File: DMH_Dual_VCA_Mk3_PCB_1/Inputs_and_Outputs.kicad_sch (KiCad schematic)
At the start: 24 parts, among them J1 TS_Jack_6.35mm_Sw, J2 TS_Jack_6.35mm_Sw, J200 IDC_02x05, J3 TS_Jack_6.35mm_Sw, J4 TS_Jack_6.35mm_Sw, J5 TS_Jack_6.35mm_Sw, J50 Conn_01x08, J6 TS_Jack_6.35mm_Sw, J60 Conn_01x08, J7 TS_Jack_6.35mm_Sw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

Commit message: Mode switching design in progress
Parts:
- removed D3: ZPD5V1, Diode_THT:D_DO-35_SOD27_P7.62mm_Horizontal, symbol Diode:ZPDxx
- removed R2: 4k7, Resistor_THT:R_Axial_DIN0207_L6.3mm_D2.5mm_P7.62mm_Horizontal, symbol Device:R_US
- R21, R40: value 20k -> 18k
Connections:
- net +5V: now reaches JP1.3 (B)

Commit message: 2nd VCA design done
Clipping design in progress
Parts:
- removed RV13: 100k, SynthStuff:Potentiometer_Alpha_RD901F-40-00D_Single_Vertical, symbol Device:R_Potentiometer_US
- added RV13: 100k, symbol Device:R_Potentiometer_Dual_Separate
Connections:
- net +5V: now also RV13.6
- net GND: now also RV13.1
- net CV P/T Jack renamed CV PT In Jack
- net CV PT In Jack: now also RV13.3
- new net -5V: RV13.4
- new net CV PT Pot G1: RV13.2
- new net CV PT Pot G2: RV13.5

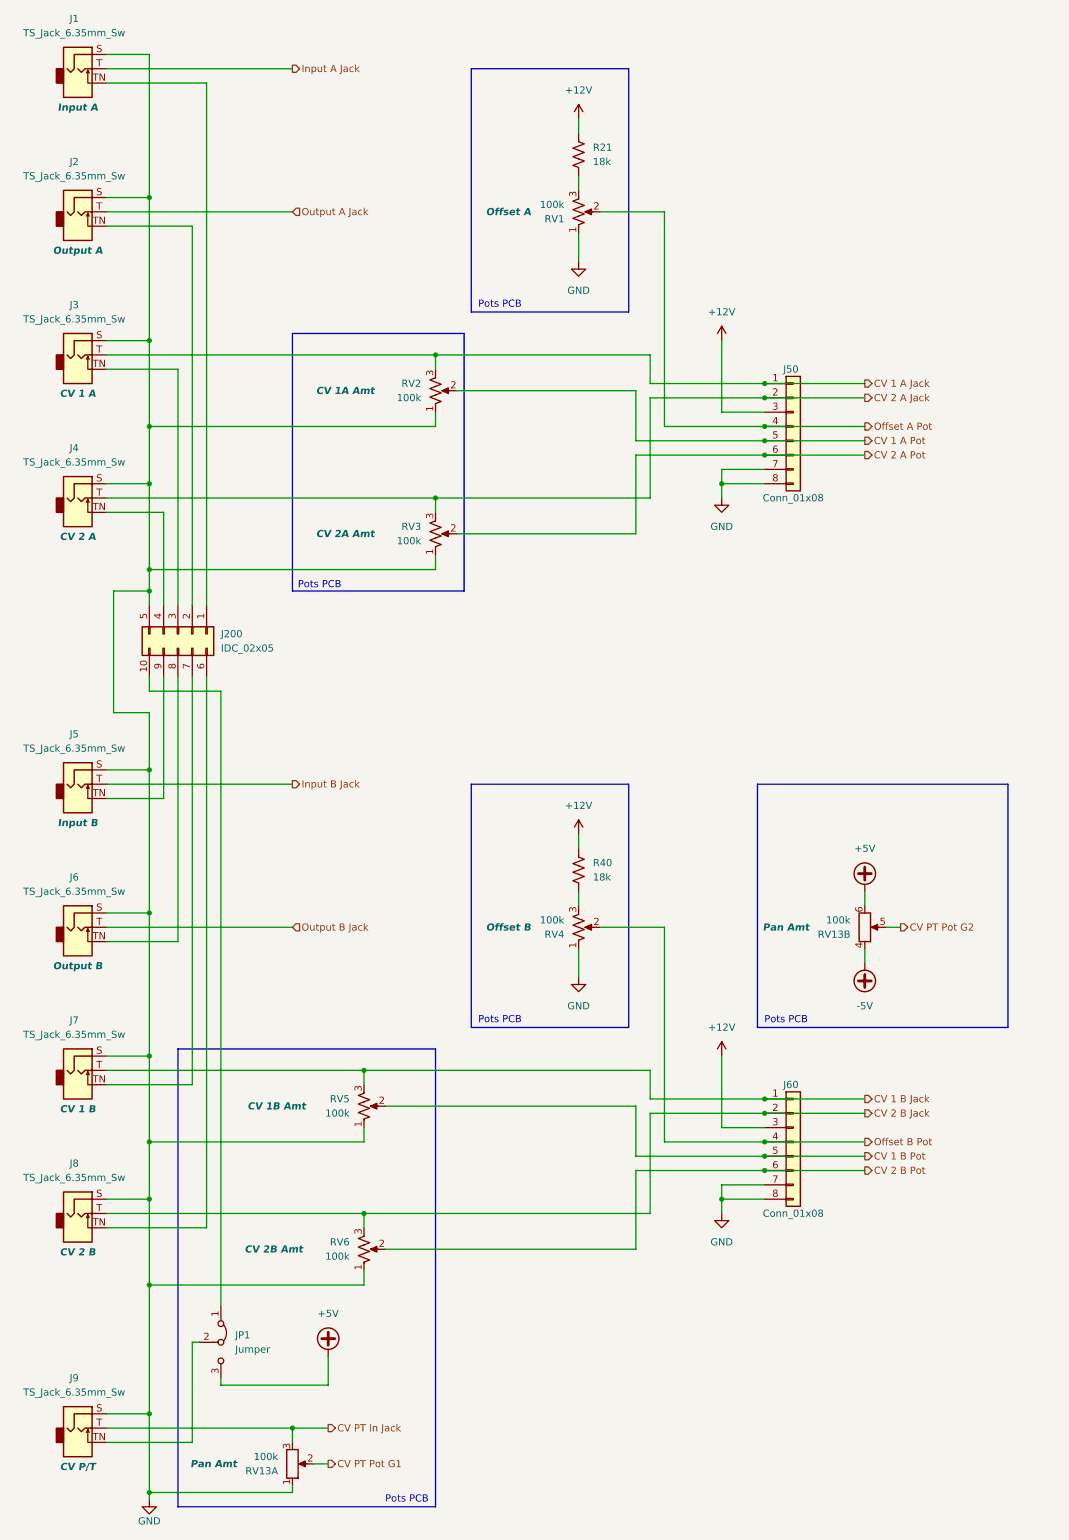
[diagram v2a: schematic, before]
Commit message: Designed clip and dist circuit
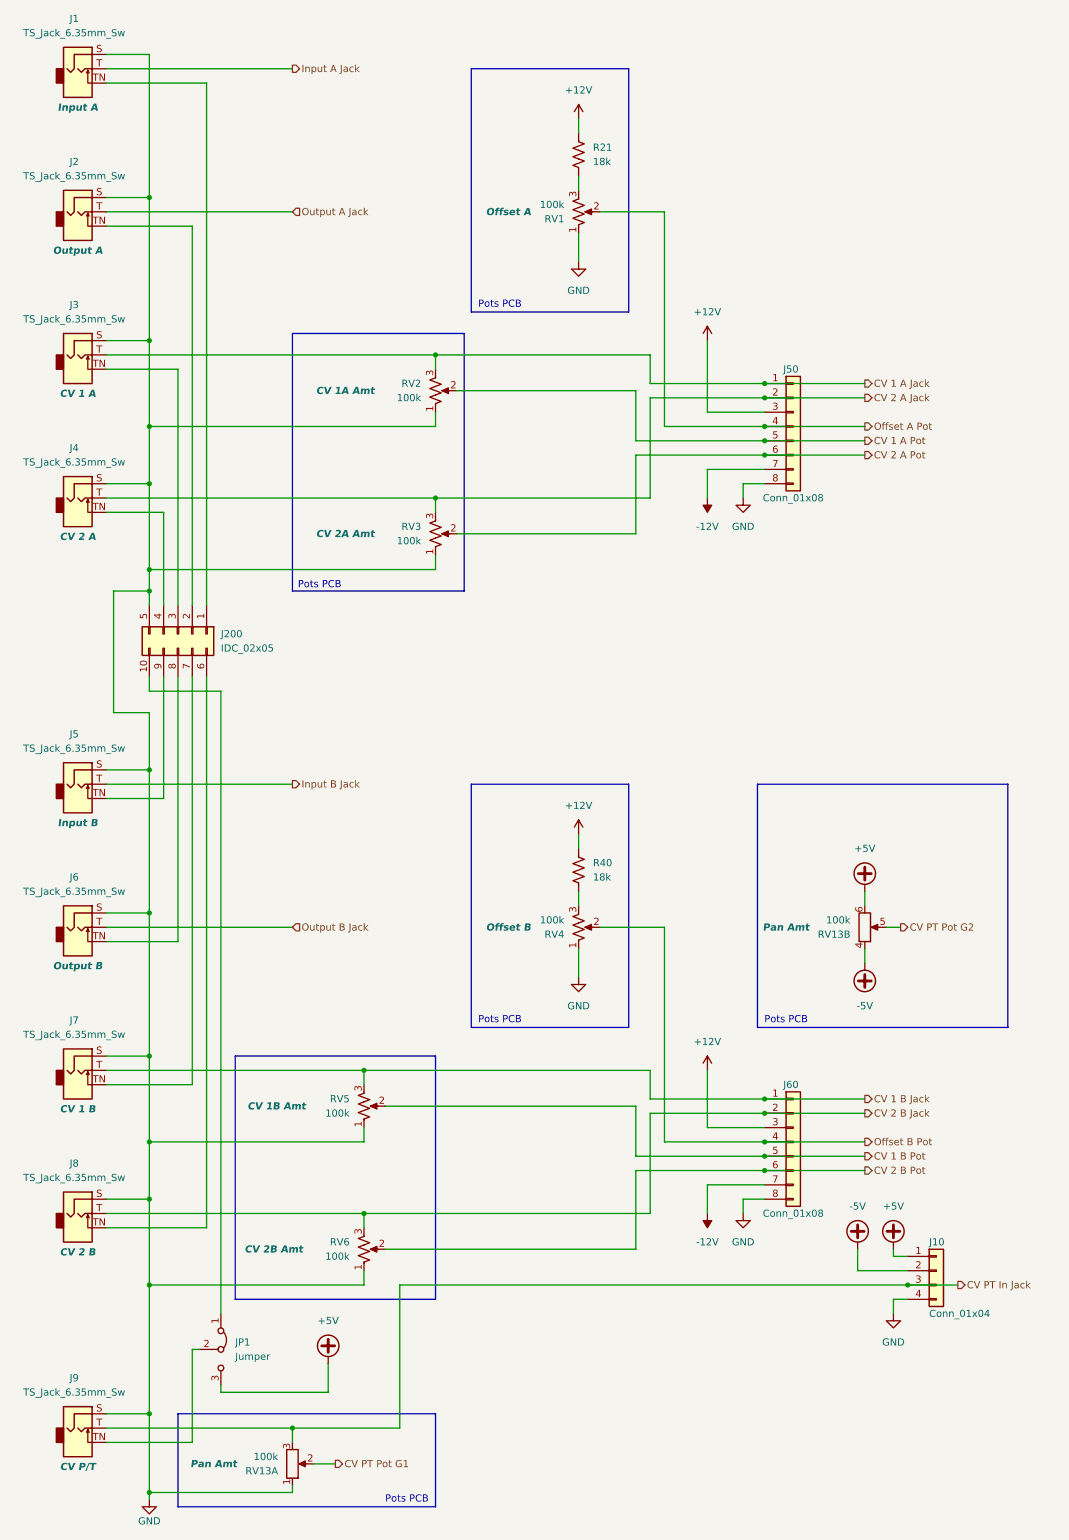
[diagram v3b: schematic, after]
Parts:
- added J10: Conn_01x04, Connector_PinHeader_2.54mm:PinHeader_1x04_P2.54mm_Vertical, symbol Connector_Generic:Conn_01x04
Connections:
- net +5V: now also J10.1 (Pin_1)
- net -5V: now also J10.2 (Pin_2)
- net CV PT In Jack: now also J10.3 (Pin_3)
- net GND: now also J10.4 (Pin_4); no longer J50.7 (Pin_7), J60.7 (Pin_7)
- new net -12V: J50.7 (Pin_7), J60.7 (Pin_7)
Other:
- moved on the sheet: JP1

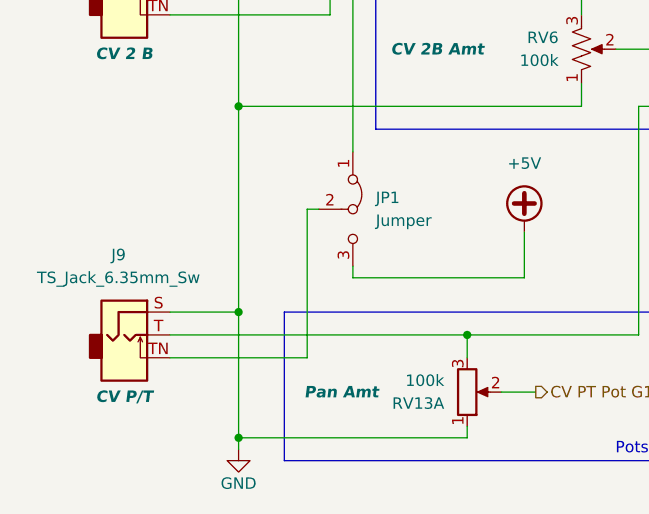
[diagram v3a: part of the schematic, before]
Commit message: Synced PCB 1 and 2 schematics
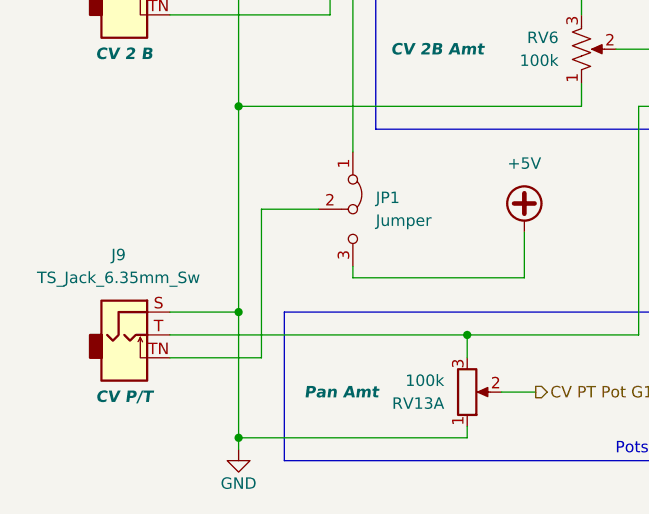
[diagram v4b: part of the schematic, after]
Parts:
- J50, J60: footprint Connector_PinSocket_2.54mm:PinSocket_1x08_P2.54mm_Vertical -> Connector_PinHeader_2.54mm:PinHeader_1x08_P2.54mm_Vertical
- JP1: footprint (none) -> Connector_PinHeader_2.54mm:PinHeader_1x03_P2.54mm_Horizontal
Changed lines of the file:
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@@
 	(wire
 		(pts
-			(xy 45.72 252.73) (xy 45.72 269.24)
+			(xy 40.64 252.73) (xy 40.64 269.24)
 		)
 		(stroke
@@
 	(wire
 		(pts
-			(xy 46.99 252.73) (xy 45.72 252.73)
+			(xy 46.99 252.73) (xy 40.64 252.73)
 		)
 		(stroke
@@
 	(wire
 		(pts
-			(xy 30.48 269.24) (xy 45.72 269.24)
+			(xy 30.48 269.24) (xy 40.64 269.24)
 		)
 		(stroke
@@
 		(exclude_from_sim no)
 		(in_bom yes)
-		(on_board yes)
+		(on_board no)
 		(dnp no)
 		(property "Reference" "RV13"
@@
 		(exclude_from_sim no)
 		(in_bom yes)
-		(on_board yes)
+		(on_board no)
 		(dnp no)
 		(property "Reference" "RV5"
@@
 		(exclude_from_sim no)
 		(in_bom yes)
-		(on_board yes)
+		(on_board no)
 		(dnp no)
 		(property "Reference" "RV6"
@@
 			)
 		)
-		(property "Footprint" "Connector_PinSocket_2.54mm:PinSocket_1x08_P2.54mm_Vertical"
+		(property "Footprint" "Connector_PinHeader_2.54mm:PinHeader_1x08_P2.54mm_Vertical"
 			(at 152.4 215.9 0)
 			(effects
@@
 		(exclude_from_sim no)
 		(in_bom yes)
-		(on_board yes)
+		(on_board no)
 		(dnp no)
 		(fields_autoplaced yes)
@@
 		(exclude_from_sim no)
 		(in_bom yes)
-		(on_board yes)
+		(on_board no)
 		(dnp no)
 		(fields_autoplaced yes)
@@
 		(exclude_from_sim no)
 		(in_bom yes)
-		(on_board yes)
+		(on_board no)
 		(dnp no)
 		(property "Reference" "RV13"
@@
 			)
 		)
-		(property "Footprint" "Connector_PinSocket_2.54mm:PinSocket_1x08_P2.54mm_Vertical"
+		(property "Footprint" "Connector_PinHeader_2.54mm:PinHeader_1x08_P2.54mm_Vertical"
 			(at 152.4 88.9 0)
 			(effects
@@
 			)
 		)
-		(property "Footprint" ""
+		(property "Footprint" "Connector_PinHeader_2.54mm:PinHeader_1x03_P2.54mm_Horizontal"
 			(at 50.8 252.73 0)
 			(effects

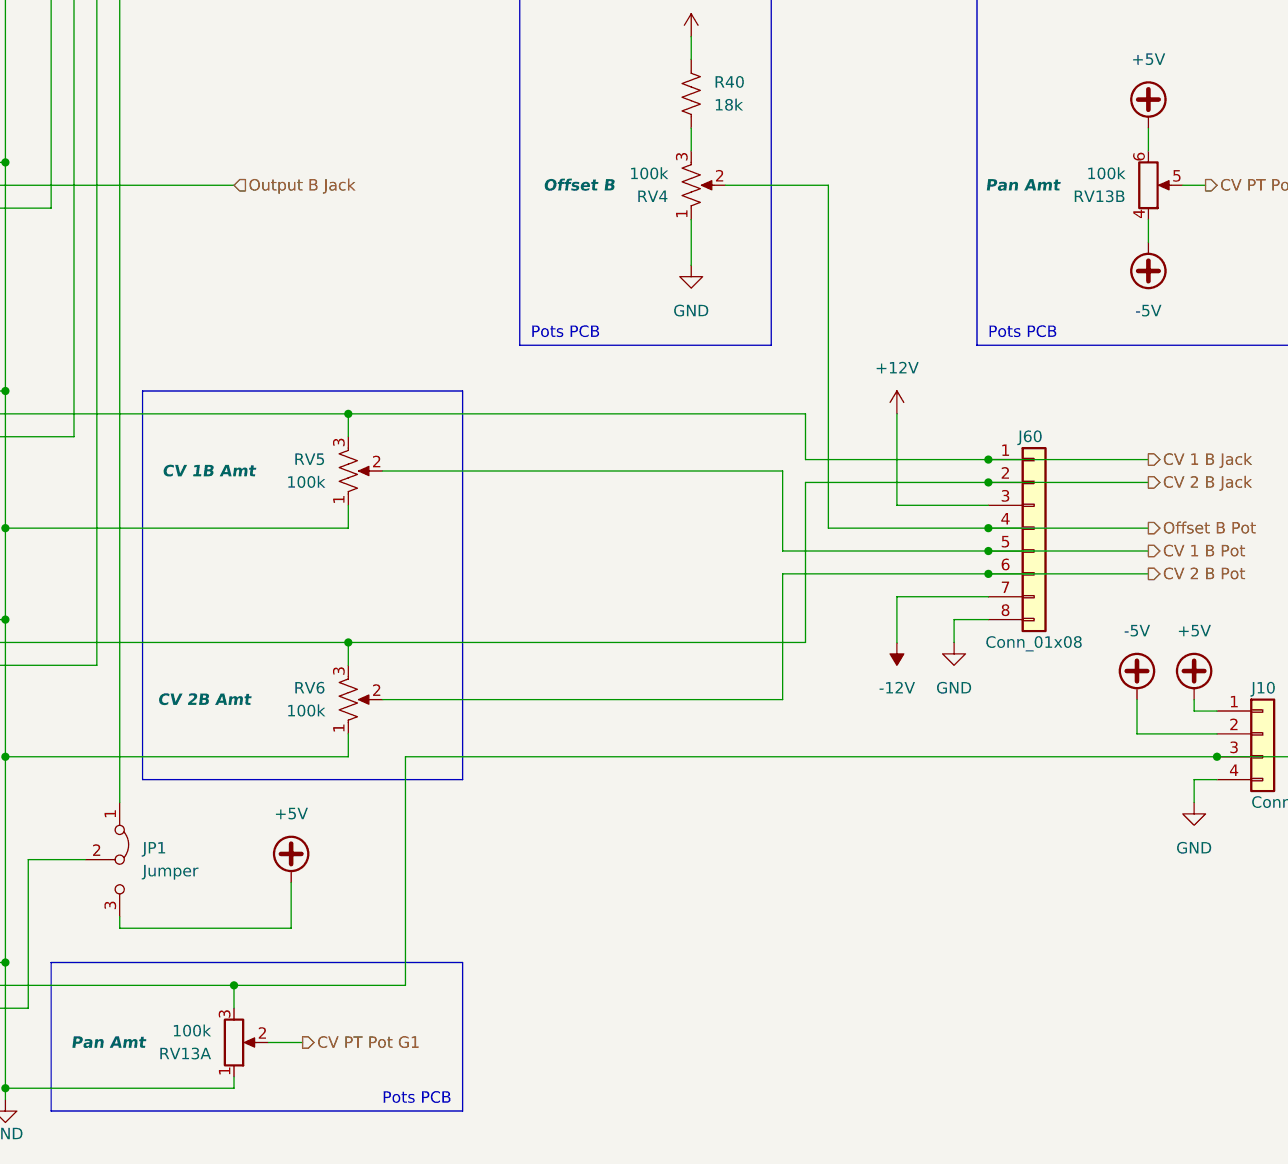
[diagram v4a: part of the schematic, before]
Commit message: Synced PCB1 to PCB2
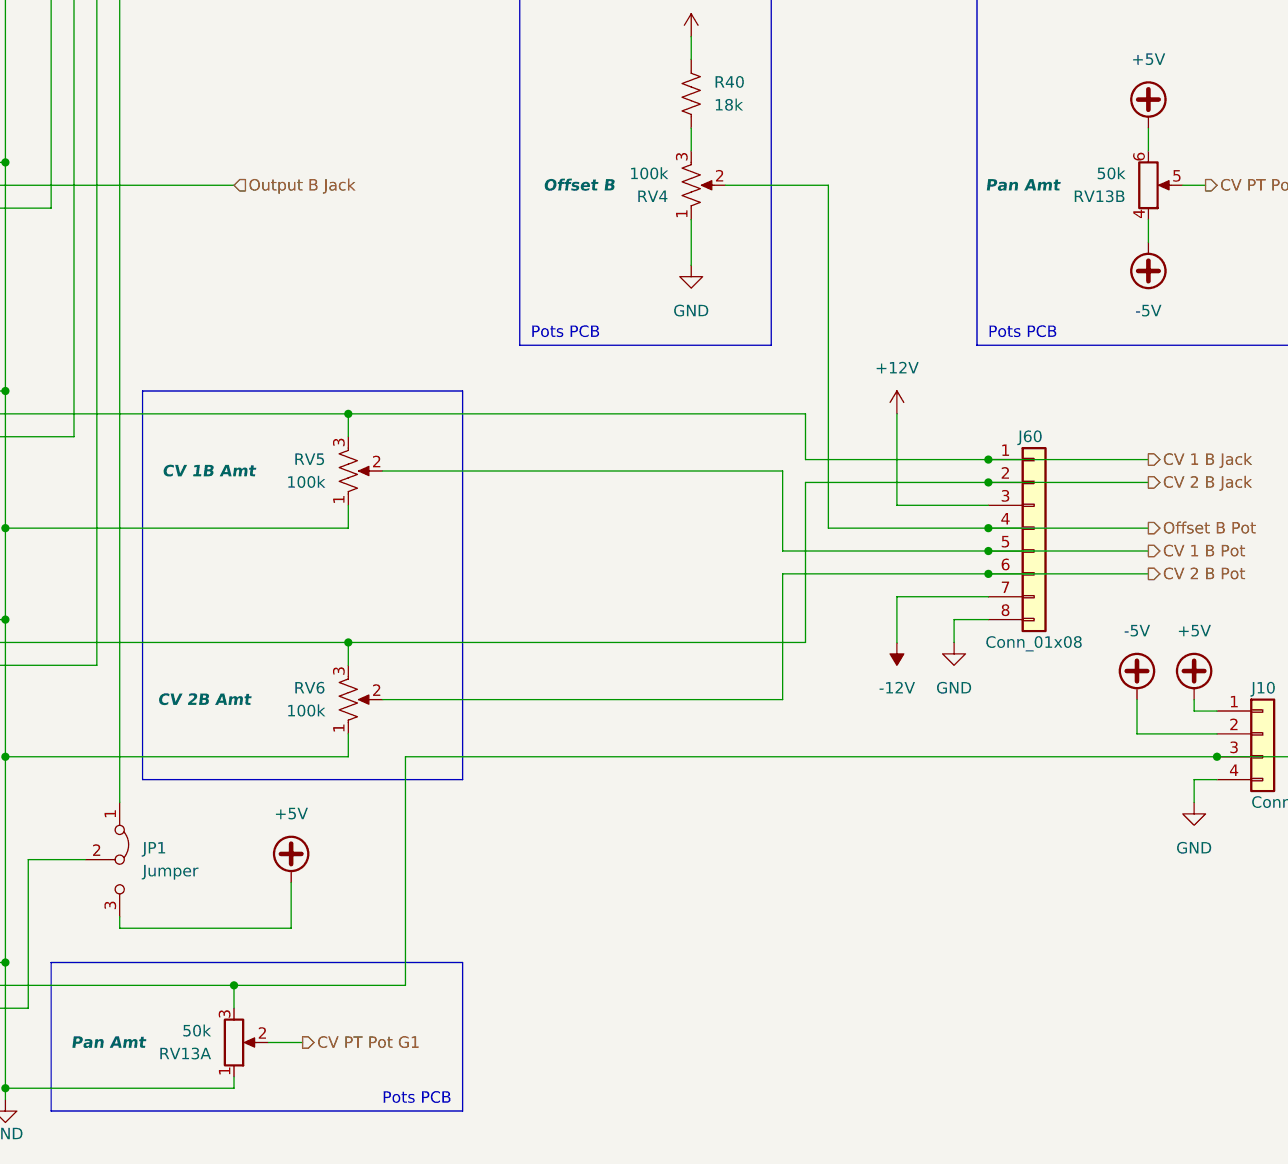
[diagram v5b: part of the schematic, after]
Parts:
- RV13: value 100k -> 50k; footprint (none) -> Potentiometer_THT:Potentiometer_Alps_RK09L_Double_Vertical
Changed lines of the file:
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@@
 			)
 		)
-		(property "Value" "100k"
+		(property "Value" "50k"
 			(at 162.56 176.5301 0)
 			(effects
@@
 			)
 		)
-		(property "Footprint" ""
+		(property "Footprint" "Potentiometer_THT:Potentiometer_Alps_RK09L_Double_Vertical"
 			(at 165.1 177.8 0)
 			(effects
@@
 			)
 		)
-		(property "Value" "100k"
+		(property "Value" "50k"
 			(at 60.96 271.7801 0)
 			(effects
@@
 			)
 		)
-		(property "Footprint" ""
+		(property "Footprint" "Potentiometer_THT:Potentiometer_Alps_RK09L_Double_Vertical"
 			(at 63.5 273.05 0)
 			(effects
